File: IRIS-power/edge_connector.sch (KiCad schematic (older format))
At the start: 5 parts

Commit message: Finalized power board V2 schematic, preparing to layout
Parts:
- removed H? (x4): MountingHole_Pad, MountingHole:MountingHole_3.2mm_M3_Pad_Via, symbol Mechanical:MountingHole_Pad
- removed J?: PCIE1X, symbol star-common-lib:PCIE1X
- added J801: IRIS_physical, star-common-lib:IRIS_Physical, symbol star-common-lib:IRIS_physical
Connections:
- net labels added: ~INT
- net labels removed: CAP_OK, DIR, ~CHRG, ~CMP_OUT
- wire segments 6 -> 10
- no-connect marks 20 -> 26
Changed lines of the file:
@@
 $Descr A4 11693 8268
 encoding utf-8
-Sheet 9 9
+Sheet 8 8
 Title ""
 Date ""
@@
 $EndDescr
 $Comp
-L star-common-lib:PCIE1X J?
-U 1 1 5F381F12
-P 5750 4050
-AR Path="/5F381F12" Ref="J?"  Part="1"
-AR Path="/5F37FC72/5F381F12" Ref="J?"  Part="1"
-F 0 "J?" H 5800 5067 50  0000 C CNN
-F 1 "PCIE1X" H 5800 4976 50  0000 C CNN
-F 2 "" H 5750 4050 50  0001 C CNN
-F 3 "" H 5750 4050 50  0001 C CNN
-	1    5750 4050
+L power:GND #PWR?
+U 1 1 5F381F34
+P 5850 5300
+AR Path="/5F381F34" Ref="#PWR?"  Part="1"
+AR Path="/5F37FC72/5F381F34" Ref="#PWR0801"  Part="1"
+F 0 "#PWR0801" H 5850 5050 50  0001 C CNN
+F 1 "GND" H 5855 5127 50  0000 C CNN
+F 2 "" H 5850 5300 50  0001 C CNN
+F 3 "" H 5850 5300 50  0001 C CNN
+	1    5850 5300
 	1    0    0    -1
 $EndComp
-NoConn ~ 5550 3350
-NoConn ~ 5550 3250
-NoConn ~ 5550 4250
-NoConn ~ 5550 4150
-NoConn ~ 5550 4050
-NoConn ~ 5550 3950
-NoConn ~ 5550 3850
-NoConn ~ 5550 3750
-NoConn ~ 5550 3650
-NoConn ~ 5550 3550
-NoConn ~ 6050 3550
-NoConn ~ 6050 3650
-NoConn ~ 6050 3750
-NoConn ~ 6050 3850
-NoConn ~ 6050 3950
-NoConn ~ 6050 4050
-NoConn ~ 6050 4150
-NoConn ~ 6050 4250
-NoConn ~ 5550 3450
-NoConn ~ 6050 3350
+Text HLabel 6250 4300 2    50   BiDi ~ 0
+SDA
+$Comp
+L star-common-lib:IRIS_physical J801
+U 1 1 5F31F1FA
+P 5850 4250
+F 0 "J801" H 5850 5317 50  0000 C CNN
+F 1 "IRIS_physical" H 5850 5226 50  0000 C CNN
+F 2 "star-common-lib:IRIS_Physical" H 5850 2950 50  0001 C CNN
+F 3 "" H 5750 4300 50  0001 C CNN
+	1    5850 4250
+	1    0    0    -1
+$EndComp
+Text HLabel 6250 3500 2    50   Input ~ 0
+~INT
 $Comp
 L power:GND #PWR?
-U 1 1 5F381F2C
-P 5450 4950
-AR Path="/5F381F2C" Ref="#PWR?"  Part="1"
-AR Path="/5F37FC72/5F381F2C" Ref="#PWR?"  Part="1"
-F 0 "#PWR?" H 5450 4700 50  0001 C CNN
-F 1 "GND" H 5455 4777 50  0000 C CNN
-F 2 "" H 5450 4950 50  0001 C CNN
-F 3 "" H 5450 4950 50  0001 C CNN
-	1    5450 4950
+U 1 1 5F352BB7
+P 6250 5100
+AR Path="/5F352BB7" Ref="#PWR?"  Part="1"
+AR Path="/5F37FC72/5F352BB7" Ref="#PWR0103"  Part="1"
+F 0 "#PWR0103" H 6250 4850 50  0001 C CNN
+F 1 "GND" H 6255 4927 50  0000 C CNN
+F 2 "" H 6250 5100 50  0001 C CNN
+F 3 "" H 6250 5100 50  0001 C CNN
+	1    6250 5100
 	1    0    0    -1
 $EndComp
 Wire Wire Line
-	5450 4950 5550 4950
+	6250 5100 6150 5100
 Wire Wire Line
-	6050 4450 6050 4350
-$Comp
-L power:GND #PWR?
-U 1 1 5F381F34
-P 6150 4950
-AR Path="/5F381F34" Ref="#PWR?"  Part="1"
-AR Path="/5F37FC72/5F381F34" Ref="#PWR?"  Part="1"
-F 0 "#PWR?" H 6150 4700 50  0001 C CNN
-F 1 "GND" H 6155 4777 50  0000 C CNN
-F 2 "" H 6150 4950 50  0001 C CNN
-F 3 "" H 6150 4950 50  0001 C CNN
-	1    6150 4950
-	1    0    0    -1
-$EndComp
+	6150 5100 6150 5000
+Connection ~ 6150 5100
+Text HLabel 6250 4900 2    50   Output ~ 0
+FB_HV_N
 Wire Wire Line
-	6050 4950 6150 4950
-Text HLabel 4700 4650 0    50   Input ~ 0
+	6250 4900 6150 4900
+Text HLabel 6250 4800 2    50   Input ~ 0
 +29.5V
-Text HLabel 4700 4450 0    50   Input ~ 0
+Wire Wire Line
+	6250 4800 6150 4800
+Text HLabel 6250 4700 2    50   Output ~ 0
+FB_HV_P
+Wire Wire Line
+	6250 4700 6150 4700
+Text HLabel 6250 4600 2    50   Input ~ 0
 VSYS
-Text HLabel 4700 4300 0    50   Input ~ 0
+Wire Wire Line
+	6250 4600 6150 4600
+Text HLabel 6250 4500 2    50   Input ~ 0
 +3.3V
-Text HLabel 4650 3900 0    50   Output ~ 0
-FB_HV_P
-Text HLabel 4650 3750 0    50   Output ~ 0
-FB_HV_N
-Text HLabel 4700 4950 0    50   Input ~ 0
-~CHRG
-Text HLabel 4650 5550 0    50   Input ~ 0
-DIR
-Text HLabel 4650 5900 0    50   Input ~ 0
-~CMP_OUT
-Text HLabel 5150 5500 0    50   Input ~ 0
-CAP_OK
-Text HLabel 8000 4200 0    50   BiDi ~ 0
-SDA
-Text HLabel 7500 4500 0    50   Output ~ 0
+Wire Wire Line
+	6250 4500 6150 4500
+Text HLabel 6250 4400 2    50   Output ~ 0
 SCL
-$Comp
-L Mechanical:MountingHole_Pad H?
-U 1 1 5F3A5F82
-P 5900 5600
-F 0 "H?" H 6000 5649 50  0000 L CNN
-F 1 "MountingHole_Pad" H 6000 5558 50  0001 L CNN
-F 2 "MountingHole:MountingHole_3.2mm_M3_Pad_Via" H 5900 5600 50  0001 C CNN
-F 3 "~" H 5900 5600 50  0001 C CNN
-	1    5900 5600
-	1    0    0    -1
-$EndComp
-Connection ~ 5900 5700
-$Comp
-L power:GND #PWR?
-U 1 1 5F3A5F89
-P 5900 5700
-F 0 "#PWR?" H 5900 5450 50  0001 C CNN
-F 1 "GND" H 5905 5527 50  0000 C CNN
-F 2 "" H 5900 5700 50  0001 C CNN
-F 3 "" H 5900 5700 50  0001 C CNN
-	1    5900 5700
-	1    0    0    -1
-$EndComp
-$Comp
-L Mechanical:MountingHole_Pad H?
-U 1 1 5F3A5F8F
-P 6900 5600
-F 0 "H?" H 7000 5649 50  0000 L CNN
-F 1 "MountingHole_Pad" H 7000 5558 50  0001 L CNN
-F 2 "MountingHole:MountingHole_3.2mm_M3_Pad_Via" H 6900 5600 50  0001 C CNN
-F 3 "~" H 6900 5600 50  0001 C CNN
-	1    6900 5600
-	1    0    0    -1
-$EndComp
 Wire Wire Line
-	6600 5700 6900 5700
-Connection ~ 6600 5700
-$Comp
-L Mechanical:MountingHole_Pad H?
-U 1 1 5F3A5F97
-P 6600 5600
-F 0 "H?" H 6700 5649 50  0000 L CNN
-F 1 "MountingHole_Pad" H 6700 5558 50  0001 L CNN
-F 2 "MountingHole:MountingHole_3.2mm_M3_Pad_Via" H 6600 5600 50  0001 C CNN
-F 3 "~" H 6600 5600 50  0001 C CNN
-	1    6600 5600
-	1    0    0    -1
-$EndComp
+	6250 4400 6150 4400
 Wire Wire Line
-	6250 5700 6600 5700
+	6250 4300 6150 4300
 Wire Wire Line
-	5900 5700 6250 5700
-Connection ~ 6250 5700
-$Comp
-L Mechanical:MountingHole_Pad H?
-U 1 1 5F3A5FA0
-P 6250 5600
-F 0 "H?" H 6350 5649 50  0000 L CNN
-F 1 "MountingHole_Pad" H 6350 5558 50  0001 L CNN
-F 2 "MountingHole:MountingHole_3.2mm_M3_Pad_Via" H 6250 5600 50  0001 C CNN
-F 3 "~" H 6250 5600 50  0001 C CNN
-	1    6250 5600
-	1    0    0    -1
-$EndComp
+	6250 3500 6150 3500
+NoConn ~ 5550 5100
+NoConn ~ 5550 5000
+NoConn ~ 5550 4900
+NoConn ~ 5550 4800
+NoConn ~ 5550 4700
+NoConn ~ 5550 4600
+NoConn ~ 5550 4500
+NoConn ~ 5550 4400
+NoConn ~ 5550 4300
+NoConn ~ 5550 4200
+NoConn ~ 5550 4100
+NoConn ~ 5550 4000
+NoConn ~ 5550 3900
+NoConn ~ 5550 3800
+NoConn ~ 5550 3700
+NoConn ~ 5550 3600
+NoConn ~ 5550 3500
+NoConn ~ 5550 3400
+NoConn ~ 6150 4200
+NoConn ~ 6150 4100
+NoConn ~ 6150 4000
+NoConn ~ 6150 3900
+NoConn ~ 6150 3800
+NoConn ~ 6150 3700
+NoConn ~ 6150 3600
+NoConn ~ 6150 3400
 $EndSCHEMATC

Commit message: Updated layout
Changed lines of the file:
@@
 P 6250 5100
 AR Path="/5F352BB7" Ref="#PWR?"  Part="1"
-AR Path="/5F37FC72/5F352BB7" Ref="#PWR0103"  Part="1"
-F 0 "#PWR0103" H 6250 4850 50  0001 C CNN
+AR Path="/5F37FC72/5F352BB7" Ref="#PWR0802"  Part="1"
+F 0 "#PWR0802" H 6250 4850 50  0001 C CNN
 F 1 "GND" H 6255 4927 50  0000 C CNN
 F 2 "" H 6250 5100 50  0001 C CNN
@@
 	6150 5100 6150 5000
 Connection ~ 6150 5100
-Text HLabel 6250 4900 2    50   Output ~ 0
+Text HLabel 6250 4800 2    50   Output ~ 0
 FB_HV_N
 Wire Wire Line
 	6250 4900 6150 4900
-Text HLabel 6250 4800 2    50   Input ~ 0
+Text HLabel 6250 4900 2    50   Input ~ 0
 +29.5V
 Wire Wire Line

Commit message: Updated layout
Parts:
- removed J801: IRIS_physical, star-common-lib:IRIS_Physical, symbol star-common-lib:IRIS_physical
- added J13: IRIS_power_board, star-common-lib:IRIS_Power_Physical, symbol star-common-lib:IRIS_power_board
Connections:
- no-connect marks 26 -> 0
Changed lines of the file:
@@
 P 5850 5300
 AR Path="/5F381F34" Ref="#PWR?"  Part="1"
-AR Path="/5F37FC72/5F381F34" Ref="#PWR0801"  Part="1"
-F 0 "#PWR0801" H 5850 5050 50  0001 C CNN
+AR Path="/5F37FC72/5F381F34" Ref="#PWR0104"  Part="1"
+F 0 "#PWR0104" H 5850 5050 50  0001 C CNN
 F 1 "GND" H 5855 5127 50  0000 C CNN
 F 2 "" H 5850 5300 50  0001 C CNN
@@
 Text HLabel 6250 4300 2    50   BiDi ~ 0
 SDA
-$Comp
-L star-common-lib:IRIS_physical J801
-U 1 1 5F31F1FA
-P 5850 4250
-F 0 "J801" H 5850 5317 50  0000 C CNN
-F 1 "IRIS_physical" H 5850 5226 50  0000 C CNN
-F 2 "star-common-lib:IRIS_Physical" H 5850 2950 50  0001 C CNN
-F 3 "" H 5750 4300 50  0001 C CNN
-	1    5850 4250
-	1    0    0    -1
-$EndComp
 Text HLabel 6250 3500 2    50   Input ~ 0
 ~INT
@@
 P 6250 5100
 AR Path="/5F352BB7" Ref="#PWR?"  Part="1"
-AR Path="/5F37FC72/5F352BB7" Ref="#PWR0802"  Part="1"
-F 0 "#PWR0802" H 6250 4850 50  0001 C CNN
+AR Path="/5F37FC72/5F352BB7" Ref="#PWR0105"  Part="1"
+F 0 "#PWR0105" H 6250 4850 50  0001 C CNN
 F 1 "GND" H 6255 4927 50  0000 C CNN
 F 2 "" H 6250 5100 50  0001 C CNN
@@
 Wire Wire Line
 	6150 5100 6150 5000
-Connection ~ 6150 5100
 Text HLabel 6250 4800 2    50   Output ~ 0
 FB_HV_N
@@
 Wire Wire Line
 	6250 3500 6150 3500
-NoConn ~ 5550 5100
-NoConn ~ 5550 5000
-NoConn ~ 5550 4900
-NoConn ~ 5550 4800
-NoConn ~ 5550 4700
-NoConn ~ 5550 4600
-NoConn ~ 5550 4500
-NoConn ~ 5550 4400
-NoConn ~ 5550 4300
-NoConn ~ 5550 4200
-NoConn ~ 5550 4100
-NoConn ~ 5550 4000
-NoConn ~ 5550 3900
-NoConn ~ 5550 3800
-NoConn ~ 5550 3700
-NoConn ~ 5550 3600
-NoConn ~ 5550 3500
-NoConn ~ 5550 3400
-NoConn ~ 6150 4200
-NoConn ~ 6150 4100
-NoConn ~ 6150 4000
-NoConn ~ 6150 3900
-NoConn ~ 6150 3800
-NoConn ~ 6150 3700
-NoConn ~ 6150 3600
-NoConn ~ 6150 3400
+Connection ~ 6150 5100
+$Comp
+L star-common-lib:IRIS_power_board J13
+U 1 1 5F4053EF
+P 5850 4250
+F 0 "J13" H 5932 5317 50  0000 C CNN
+F 1 "IRIS_power_board" H 5932 5226 50  0000 C CNN
+F 2 "star-common-lib:IRIS_Power_Physical" H 5850 2950 50  0001 C CNN
+F 3 "" H 5750 4300 50  0001 C CNN
+	1    5850 4250
+	1    0    0    -1
+$EndComp
 $EndSCHEMATC

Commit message: Begin revising for IRIS V4
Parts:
- removed J13: IRIS_power_board, star-common-lib:IRIS_Power_Physical, symbol star-common-lib:IRIS_power_board
- added J13: Conn_01x20_MountingPin, star-common-lib:IRIS_Muons_physical, symbol Connector_Generic_MountingPin:Conn_01x20_MountingPin
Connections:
- wire segments 10 -> 12
- no-connect marks 0 -> 8
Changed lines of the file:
@@
 Comment4 ""
 $EndDescr
-$Comp
-L power:GND #PWR?
-U 1 1 5F381F34
-P 5850 5300
-AR Path="/5F381F34" Ref="#PWR?"  Part="1"
-AR Path="/5F37FC72/5F381F34" Ref="#PWR0104"  Part="1"
-F 0 "#PWR0104" H 5850 5050 50  0001 C CNN
-F 1 "GND" H 5855 5127 50  0000 C CNN
-F 2 "" H 5850 5300 50  0001 C CNN
-F 3 "" H 5850 5300 50  0001 C CNN
-	1    5850 5300
-	1    0    0    -1
-$EndComp
-Text HLabel 6250 4300 2    50   BiDi ~ 0
+Text HLabel 5700 3600 2    50   BiDi ~ 0
 SDA
-Text HLabel 6250 3500 2    50   Input ~ 0
+Text HLabel 5700 3100 2    50   Input ~ 0
 ~INT
 $Comp
 L power:GND #PWR?
 U 1 1 5F352BB7
-P 6250 5100
+P 5800 4800
 AR Path="/5F352BB7" Ref="#PWR?"  Part="1"
 AR Path="/5F37FC72/5F352BB7" Ref="#PWR0105"  Part="1"
-F 0 "#PWR0105" H 6250 4850 50  0001 C CNN
-F 1 "GND" H 6255 4927 50  0000 C CNN
-F 2 "" H 6250 5100 50  0001 C CNN
-F 3 "" H 6250 5100 50  0001 C CNN
-	1    6250 5100
+F 0 "#PWR0105" H 5800 4550 50  0001 C CNN
+F 1 "GND" H 5805 4627 50  0000 C CNN
+F 2 "" H 5800 4800 50  0001 C CNN
+F 3 "" H 5800 4800 50  0001 C CNN
+	1    5800 4800
+	1    0    0    -1
+$EndComp
+Text HLabel 5700 4500 2    50   Output ~ 0
+FB_HV_N
+Wire Wire Line
+	5700 4600 5600 4600
+Text HLabel 5700 4600 2    50   Input ~ 0
++29.5V
+Wire Wire Line
+	5700 4500 5600 4500
+Text HLabel 5700 4400 2    50   Output ~ 0
+FB_HV_P
+Wire Wire Line
+	5700 4400 5600 4400
+Text HLabel 5700 4300 2    50   Input ~ 0
+VSYS
+Wire Wire Line
+	5700 4300 5600 4300
+Text HLabel 5700 4200 2    50   Input ~ 0
++3.3V
+Wire Wire Line
+	5700 4200 5600 4200
+Text HLabel 5700 3700 2    50   Output ~ 0
+SCL
+Wire Wire Line
+	5700 3700 5600 3700
+Wire Wire Line
+	5700 3600 5600 3600
+Wire Wire Line
+	5700 3100 5600 3100
+$Comp
+L Connector_Generic_MountingPin:Conn_01x20_MountingPin J13
+U 1 1 5F8510FD
+P 5400 3800
+F 0 "J13" H 5322 4917 50  0000 C CNN
+F 1 "Conn_01x20_MountingPin" H 5322 4826 50  0000 C CNN
+F 2 "star-common-lib:IRIS_Muons_physical" H 5400 3800 50  0001 C CNN
+F 3 "~" H 5400 3800 50  0001 C CNN
+	1    5400 3800
+	-1   0    0    -1
+$EndComp
+Wire Wire Line
+	5600 4800 5800 4800
+Wire Wire Line
+	5600 4800 5600 4700
+Connection ~ 5600 4800
+$Comp
+L power:GND #PWR0104
+U 1 1 5F854DB8
+P 6100 4100
+F 0 "#PWR0104" H 6100 3850 50  0001 C CNN
+F 1 "GND" H 6105 3927 50  0000 C CNN
+F 2 "" H 6100 4100 50  0001 C CNN
+F 3 "" H 6100 4100 50  0001 C CNN
+	1    6100 4100
 	1    0    0    -1
 $EndComp
 Wire Wire Line
-	6250 5100 6150 5100
-Wire Wire Line
-	6150 5100 6150 5000
-Text HLabel 6250 4800 2    50   Output ~ 0
-FB_HV_N
-Wire Wire Line
-	6250 4900 6150 4900
-Text HLabel 6250 4900 2    50   Input ~ 0
-+29.5V
-Wire Wire Line
-	6250 4800 6150 4800
-Text HLabel 6250 4700 2    50   Output ~ 0
-FB_HV_P
-Wire Wire Line
-	6250 4700 6150 4700
-Text HLabel 6250 4600 2    50   Input ~ 0
-VSYS
-Wire Wire Line
-	6250 4600 6150 4600
-Text HLabel 6250 4500 2    50   Input ~ 0
-+3.3V
-Wire Wire Line
-	6250 4500 6150 4500
-Text HLabel 6250 4400 2    50   Output ~ 0
-SCL
-Wire Wire Line
-	6250 4400 6150 4400
-Wire Wire Line
-	6250 4300 6150 4300
-Wire Wire Line
-	6250 3500 6150 3500
-Connection ~ 6150 5100
+	6100 4100 5600 4100
 $Comp
-L star-common-lib:IRIS_power_board J13
-U 1 1 5F4053EF
-P 5850 4250
-F 0 "J13" H 5932 5317 50  0000 C CNN
-F 1 "IRIS_power_board" H 5932 5226 50  0000 C CNN
-F 2 "star-common-lib:IRIS_Power_Physical" H 5850 2950 50  0001 C CNN
-F 3 "" H 5750 4300 50  0001 C CNN
-	1    5850 4250
+L power:GND #PWR0107
+U 1 1 5F8554EB
+P 6100 2900
+F 0 "#PWR0107" H 6100 2650 50  0001 C CNN
+F 1 "GND" H 6105 2727 50  0000 C CNN
+F 2 "" H 6100 2900 50  0001 C CNN
+F 3 "" H 6100 2900 50  0001 C CNN
+	1    6100 2900
 	1    0    0    -1
 $EndComp
+Wire Wire Line
+	5600 2900 6100 2900
+NoConn ~ 5600 3800
+NoConn ~ 5600 3900
+NoConn ~ 5600 4000
+NoConn ~ 5600 3500
+NoConn ~ 5600 3400
+NoConn ~ 5600 3300
+NoConn ~ 5600 3200
+NoConn ~ 5600 3000
+$Comp
+L power:GND #PWR?
+U 1 1 5F856D4C
+P 5400 5000
+AR Path="/5F856D4C" Ref="#PWR?"  Part="1"
+AR Path="/5F37FC72/5F856D4C" Ref="#PWR0108"  Part="1"
+F 0 "#PWR0108" H 5400 4750 50  0001 C CNN
+F 1 "GND" H 5405 4827 50  0000 C CNN
+F 2 "" H 5400 5000 50  0001 C CNN
+F 3 "" H 5400 5000 50  0001 C CNN
+	1    5400 5000
+	1    0    0    -1
+$EndComp

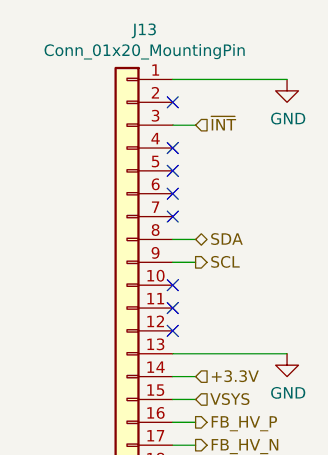
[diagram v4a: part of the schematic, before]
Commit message: Updated IRIS power board for V4
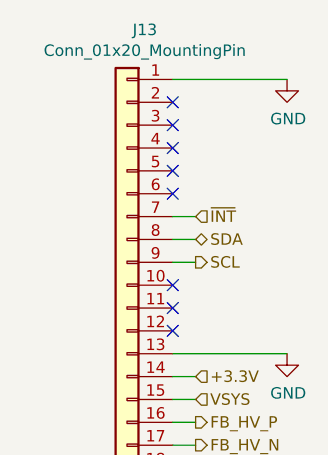
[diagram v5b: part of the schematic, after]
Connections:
- net ~INT: now also J13.7 (Pin_7); no longer J13.3 (Pin_3)
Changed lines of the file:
@@
 Text HLabel 5700 3600 2    50   BiDi ~ 0
 SDA
-Text HLabel 5700 3100 2    50   Input ~ 0
+Text HLabel 5700 3500 2    50   Input ~ 0
 ~INT
 $Comp
@@
 	5700 3600 5600 3600
 Wire Wire Line
-	5700 3100 5600 3100
+	5700 3500 5600 3500
 $Comp
 L Connector_Generic_MountingPin:Conn_01x20_MountingPin J13
@@
 NoConn ~ 5600 3900
 NoConn ~ 5600 4000
-NoConn ~ 5600 3500
+NoConn ~ 5600 3100
 NoConn ~ 5600 3400
 NoConn ~ 5600 3300

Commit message: Updated to V4.01
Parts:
- J13: footprint star-common-lib:IRIS_Muons_physical -> star-common-lib:IRIS_V4_power
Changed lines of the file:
@@
 F 0 "J13" H 5322 4917 50  0000 C CNN
 F 1 "Conn_01x20_MountingPin" H 5322 4826 50  0000 C CNN
-F 2 "star-common-lib:IRIS_Muons_physical" H 5400 3800 50  0001 C CNN
+F 2 "star-common-lib:IRIS_V4_power" H 5400 3800 50  0001 C CNN
 F 3 "~" H 5400 3800 50  0001 C CNN
 	1    5400 3800
